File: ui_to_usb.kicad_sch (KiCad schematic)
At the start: 35 parts, among them J1 PM254-2-06-S-8.5, J2 TYPE-C-31-M-12, U1 FT232H, U2 93LCxxB, U3 USBLC6-2SC6, Y2 12M

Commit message: add silkscreen
fix all DRC errors
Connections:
- no-connect marks 2 -> 11
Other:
- moved on the sheet: C1, C5

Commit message: bigger cut-out for LEDs. Add README and renders
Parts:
- D1, D2: footprint LED_SMD:LED_1206_3216Metric_ReverseMount_Hole1.8x2.4mm -> footprints:LED_1206_3216Metric_ReverseMount_Hole2.0x1.6mm

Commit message: check sch and pcb before production, looks ready
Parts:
- R5, R6: value 220R -> 1k5
- R7, R8: value 10k -> 5k1
- U2: value 93LCxxB -> 93LC56B
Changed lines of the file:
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@@
 			)
 		)
-		(property "Value" "93LCxxB"
+		(property "Value" "93LC56B"
 			(at 84.6933 116.84 0)
 			(effects
@@
 			)
 		)
-		(property "Value" "10k"
+		(property "Value" "5k1"
 			(at 62.23 49.53 90)
 			(effects
@@
 			)
 		)
-		(property "Value" "10k"
+		(property "Value" "5k1"
 			(at 62.23 46.99 90)
 			(effects
@@
 			)
 		)
-		(property "Value" "220R"
+		(property "Value" "1k5"
 			(at 198.12 132.08 90)
 			(effects
@@
 			)
 		)
-		(property "Value" "220R"
+		(property "Value" "1k5"
 			(at 198.12 146.05 90)
 			(effects

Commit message: improve BOM, ordered rev -
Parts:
- removed U2: 93LC56B, Package_SO:SOIC-8_3.9x4.9mm_P1.27mm, symbol Memory_EEPROM:93LCxxB
- added U2: 93LC56C, Package_SO:SOIC-8_3.9x4.9mm_P1.27mm, symbol Memory_EEPROM:93LCxxC
- FB1, FB2, FB3, FB4: JLCPCB Part # (none) -> C19330
- U1: footprint Package_QFP:LQFP-48_7x7mm_P0.5mm -> Package_DFN_QFN:QFN-48-1EP_8x8mm_P0.5mm_EP6.2x6.2mm
- Y2: JLCPCB Part # (none) -> C9002
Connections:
- net +3.3V: now also U2.6 (ORG), U2.8 (VCC)
- net EECLK: now also U2.2 (SCLK)
- net EECS: now also U2.1 (CS)
- net GND: now also U2.5 (GND)
- net at R3.2, U1.43 (EEDATA): now also U2.3 (DI)
- net at R3.1, R4.1: now also U2.4 (DO)
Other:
- note added: "16 bit mode"
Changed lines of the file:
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@@
 		(comment 1 "USB adapter for ui_board_1u")
 	)
+	(text "16 bit\nmode"
+		(exclude_from_sim no)
+		(at 73.914 128.27 0)
+		(effects
+			(font
+				(size 1.27 1.27)
+			)
+			(justify right)
+		)
+	)
 	(junction
 		(at 67.31 35.56)
@@
 	)
 	(symbol
-		(lib_id "Memory_EEPROM:93LCxxB")
-		(at 82.55 124.46 0)
-		(unit 1)
-		(exclude_from_sim no)
-		(in_bom yes)
-		(on_board yes)
-		(dnp no)
-		(fields_autoplaced yes)
-		(property "Reference" "U2"
-			(at 84.6933 114.3 0)
-			(effects
-				(font
-					(size 1.27 1.27)
-				)
-				(justify left)
-			)
-		)
-		(property "Value" "93LC56B"
-			(at 84.6933 116.84 0)
-			(effects
-				(font
-					(size 1.27 1.27)
-				)
-				(justify left)
-			)
-		)
-		(property "Footprint" "Package_SO:SOIC-8_3.9x4.9mm_P1.27mm"
-			(at 82.55 124.46 0)
-			(effects
-				(font
-					(size 1.27 1.27)
-				)
-				(hide yes)
-			)
-		)
-		(property "Datasheet" "http://ww1.microchip.com/downloads/en/DeviceDoc/20001749K.pdf"
-			(at 82.55 124.46 0)
-			(effects
-				(font
-					(size 1.27 1.27)
-				)
-				(hide yes)
-			)
-		)
-		(property "Description" "Serial EEPROM, 93 Series, 2.5V, DIP-8/SOIC-8"
-			(at 82.55 124.46 0)
-			(effects
-				(font
-					(size 1.27 1.27)
-				)
-				(hide yes)
-			)
-		)
-		(property "LCSC Part #" ""
-			(at 82.55 124.46 0)
-			(effects
-				(font
-					(size 1.27 1.27)
-				)
-				(hide yes)
-			)
-		)
-		(pin "8"
-		)
-		(pin "7"
-		)
-		(pin "4"
-		)
-		(pin "6"
-		)
-		(pin "5"
-		)
-		(pin "2"
-		)
-		(pin "3"
-		)
-		(pin "1"
-		)
-		(instances
-			(project ""
-				(path "/61164785-2abe-4800-8948-e7ba22968736"
-					(reference "U2")
-					(unit 1)
-				)
-			)
-		)
-	)
-	(symbol
 		(lib_id "power:PWR_FLAG")
 		(at 127 88.9 90)
@@
 			)
 		)
-		(property "Description" "BLM18AG601SN1D"
+		(property "Description" ""
 			(at 154.94 60.96 0)
 			(effects
@@
 			)
 		)
-		(property "LCSC Part #" ""
+		(property "JLCPCB Part #" "C19330"
 			(at 154.94 60.96 0)
 			(effects
@@
 			)
 		)
-		(property "Footprint" "Package_QFP:LQFP-48_7x7mm_P0.5mm"
+		(property "Footprint" "Package_DFN_QFN:QFN-48-1EP_8x8mm_P0.5mm_EP6.2x6.2mm"
 			(at 154.94 116.84 0)
 			(effects
@@
 			)
 		)
-		(property "Description" "BLM18AG601SN1D"
+		(property "Description" ""
 			(at 62.23 41.91 0)
 			(effects
@@
 			)
 		)
-		(property "LCSC Part #" ""
+		(property "JLCPCB Part #" "C19330"
 			(at 62.23 41.91 90)
 			(effects
@@
 			)
 		)
-		(property "LCSC Part #" ""
+		(property "JLCPCB Part #" "C9002"
 			(at 127 134.62 90)
 			(effects
@@
 			)
 		)
-		(property "Description" "BLM18AG601SN1D"
+		(property "Description" ""
 			(at 143.51 60.96 0)
 			(effects
@@
 			)
 		)
-		(property "LCSC Part #" ""
+		(property "JLCPCB Part #" "C19330"
 			(at 143.51 60.96 0)
 			(effects
@@
 	)
 	(symbol
+		(lib_id "Memory_EEPROM:93LCxxC")
+		(at 82.55 124.46 0)
+		(unit 1)
+		(exclude_from_sim no)
+		(in_bom yes)
+		(on_board yes)
+		(dnp no)
+		(property "Reference" "U2"
+			(at 88.138 115.316 0)
+			(effects
+				(font
+					(size 1.27 1.27)
+				)
+				(justify left)
+			)
+		)
+		(property "Value" "93LC56C"
+			(at 88.138 117.856 0)
+			(effects
+				(font
+					(size 1.27 1.27)
+				)
+				(justify left)
+			)
+		)
+		(property "Footprint" "Package_SO:SOIC-8_3.9x4.9mm_P1.27mm"
+			(at 82.55 124.46 0)
+			(effects
+				(font
+					(size 1.27 1.27)
+				)
+				(hide yes)
+			)
+		)
+		(property "Datasheet" "http://ww1.microchip.com/downloads/en/DeviceDoc/20001749K.pdf"
+			(at 82.55 124.46 0)
+			(effects
+				(font
+					(size 1.27 1.27)
+				)
+				(hide yes)
+			)
+		)
+		(property "Description" "Serial EEPROM, 93 Series, with ORG Pin, 2.5V, DIP-8/SOIC-8"
+			(at 82.55 124.46 0)
+			(effects
+				(font
+					(size 1.27 1.27)
+				)
+				(hide yes)
+			)
+		)
+		(pin "1"
+		)
+		(pin "7"
+		)
+		(pin "3"
+		)
+		(pin "5"
+		)
+		(pin "2"
+		)
+		(pin "8"
+		)
+		(pin "6"
+		)
+		(pin "4"
+		)
+		(instances
+			(project ""
+				(path "/61164785-2abe-4800-8948-e7ba22968736"
+					(reference "U2")
+					(unit 1)
+				)
+			)
+		)
+	)
+	(symbol
 		(lib_id "power:GND")
 		(at 114.3 129.54 270)
@@
 	(symbol
 		(lib_id "power:+3.3V")
+		(at 72.39 124.46 90)
+		(unit 1)
+		(exclude_from_sim no)
+		(in_bom yes)
+		(on_board yes)
+		(dnp no)
+		(property "Reference" "#PWR051"
+			(at 76.2 124.46 0)
+			(effects
+				(font
+					(size 1.27 1.27)
+				)
+				(hide yes)
+			)
+		)
+		(property "Value" "+3.3V"
+			(at 66.548 124.206 90)
+			(effects
+				(font
+					(size 1.27 1.27)
+				)
+			)
+		)
+		(property "Footprint" ""
+			(at 72.39 124.46 0)
+			(effects
+				(font
+					(size 1.27 1.27)
+				)
+				(hide yes)
+			)
+		)
+		(property "Datasheet" ""
+			(at 72.39 124.46 0)
+			(effects
+				(font
+					(size 1.27 1.27)
+				)
+				(hide yes)
+			)
+		)
+		(property "Description" "Power symbol creates a global label with name \"+3.3V\""
+			(at 72.39 124.46 0)
+			(effects
+				(font
+					(size 1.27 1.27)
+				)
+				(hide yes)
+			)
+		)
+		(pin "1"
+		)
+		(instances
+			(project "ui_to_usb"
+				(path "/61164785-2abe-4800-8948-e7ba22968736"
+					(reference "#PWR051")
+					(unit 1)
+				)
+			)
+		)
+	)
+	(symbol
+		(lib_id "power:+3.3V")
 		(at 160.02 78.74 0)
 		(unit 1)
@@
 			)
 		)
-		(property "Description" "BLM18AG601SN1D"
+		(property "Description" ""
 			(at 62.23 35.56 0)
 			(effects
@@
 			)
 		)
-		(property "LCSC Part #" ""
+		(property "JLCPCB Part #" "C19330"
 			(at 62.23 35.56 90)
 			(effects

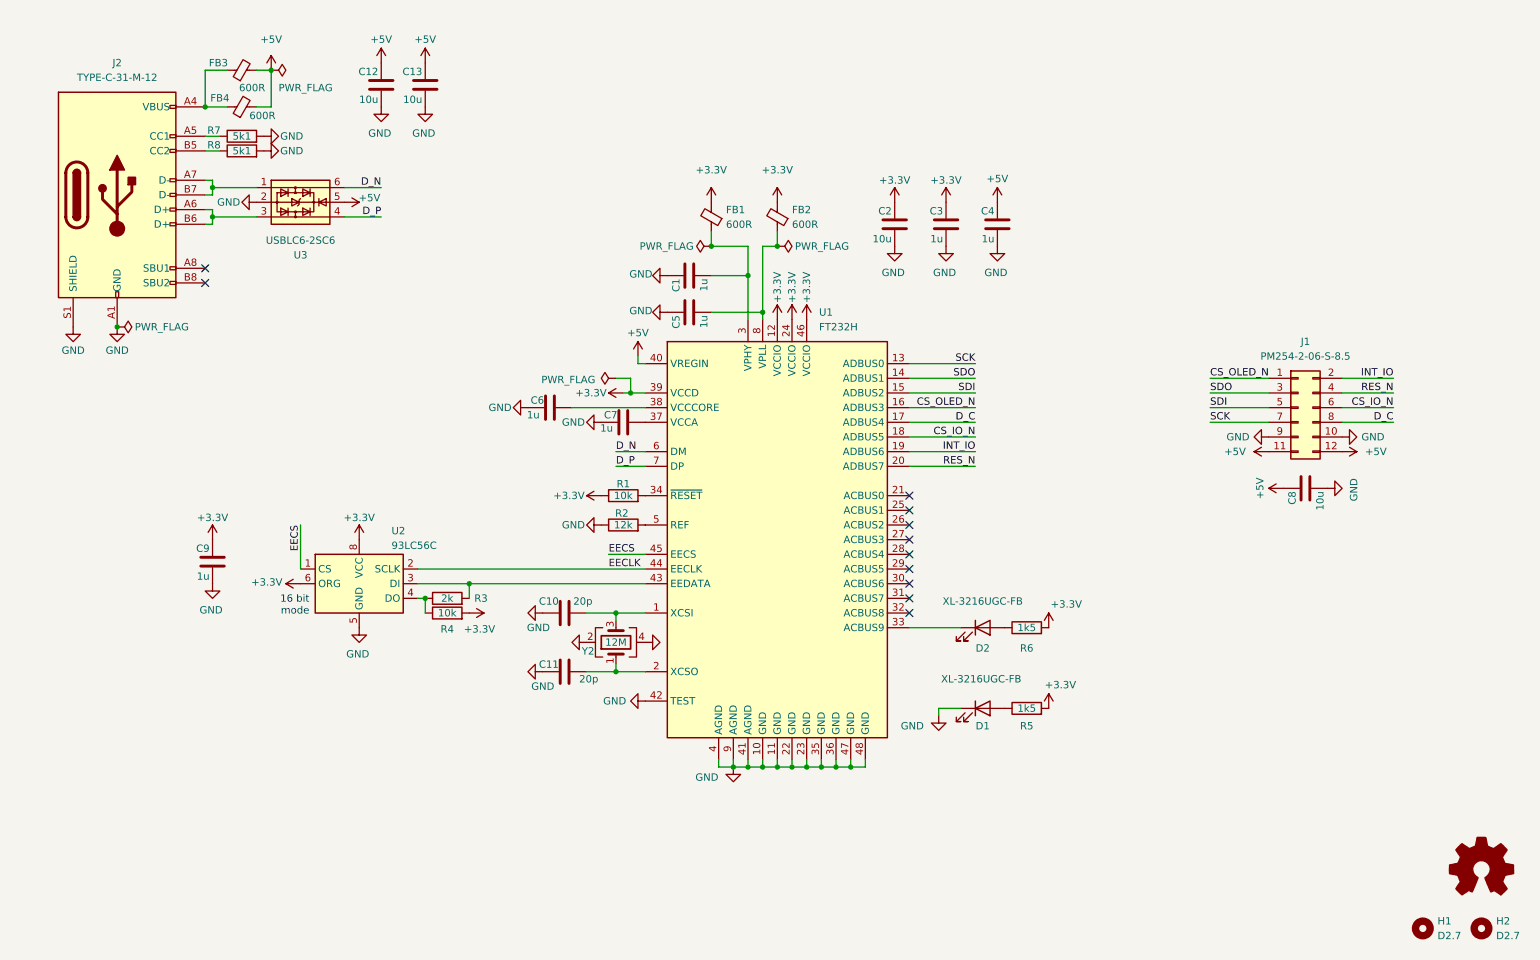
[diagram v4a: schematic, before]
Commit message: add CH32V305G (QFN28) symbol
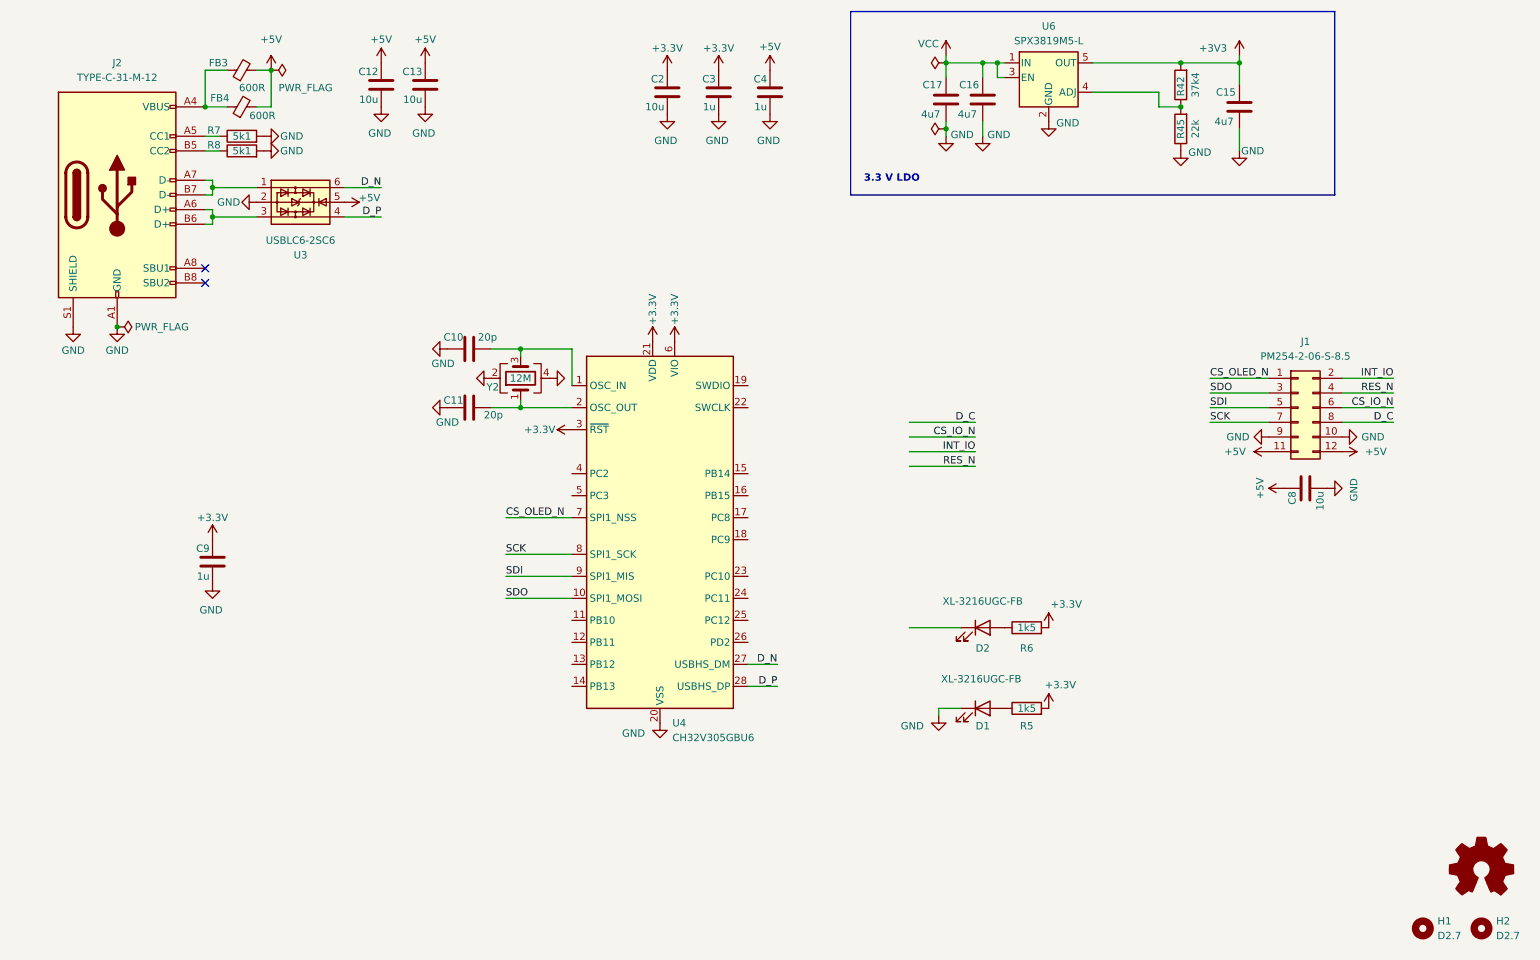
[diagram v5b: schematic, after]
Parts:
- removed C1, C5, C6, C7: 1u, Capacitor_SMD:C_0603_1608Metric, symbol Device:C
- removed FB1, FB2: 600R, Inductor_SMD:L_0603_1608Metric, symbol Device:FerriteBead_Small
- removed R1, R4: 10k, Resistor_SMD:R_0603_1608Metric, symbol Device:R
- removed R2: 12k, Resistor_SMD:R_0603_1608Metric, symbol Device:R
- removed R3: 2k, Resistor_SMD:R_0603_1608Metric, symbol Device:R
- removed U1: FT232H, Package_DFN_QFN:QFN-48-1EP_8x8mm_P0.5mm_EP6.2x6.2mm, symbol Interface_USB:FT232H
- removed U2: 93LC56C, Package_SO:SOIC-8_3.9x4.9mm_P1.27mm, symbol Memory_EEPROM:93LCxxC
- added C15, C16, C17: 4u7, Capacitor_SMD:C_1206_3216Metric, symbol Device:C
- added R42: 37k4, Resistor_SMD:R_0603_1608Metric, symbol Device:R
- added R45: 22k, Resistor_SMD:R_0603_1608Metric, symbol Device:R
- added U4: CH32V305GBU6, Package_DFN_QFN:QFN-28-1EP_4x4mm_P0.4mm_EP2.3x2.3mm, symbol lib:CH32V305GBU6
- added U6: SPX3819M5-L, Package_TO_SOT_SMD:SOT-23-5, symbol Regulator_Linear:SPX3819M5-L
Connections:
- net +3.3V: now also U4.21 (VDD), U4.3 (~{RST}), U4.6 (VIO)
- net CS_OLED_N: now also U4.7 (PA4)
- net D_N: now also U4.27 (PB6)
- net D_P: now also U4.28 (PB7)
- net GND: now also C15.2, C16.2, C17.2, R45.1, U4.0 (VSS), U4.20 (VSS), U6.2 (GND)
- net SCK: now also U4.8 (PA5)
- net SDI: now also U4.9 (PA6)
- net SDO: now also U4.10 (PA7)
- net at C10.2, Y2.3: now also U4.1 (OSC_IN)
- net at C11.2, Y2.1: now also U4.2 (OSC_OUT)
- new net: R42.1, R45.2, U6.4 (ADJ)
- new net +3V3: C15.1, R42.2, U6.5 (OUT)
- new net VCC: C16.1, C17.1, U6.1 (IN), U6.3 (EN)
- no-connect marks 11 -> 2
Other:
- note added: "3.3 V LDO"
- note removed: "16 bit mode"
- moved on the sheet: C10, C11, C2, C3, C4, Y2

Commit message: schematic progress
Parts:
- Y2: value 12M -> 8M; JLCPCB Part # C9002 -> C2682774
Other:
- note added: "ADD Buttons * RESET * BOOTLOAD"
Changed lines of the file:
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@@
 		)
 	)
+	(text "ADD Buttons\n  * RESET\n  * BOOTLOAD"
+		(exclude_from_sim no)
+		(at 134.874 164.846 0)
+		(effects
+			(font
+				(size 1.27 1.27)
+			)
+			(justify left)
+		)
+	)
 	(text "3.3 V LDO"
 		(exclude_from_sim no)
@@
 			)
 		)
-		(property "Value" "12M"
+		(property "Value" "8M"
 			(at 110.49 88.9 90)
 			(effects
@@
 			)
 		)
-		(property "Datasheet" "https://jlcpcb.com/partdetail/YXC_CrystalOscillators-X322512MSB4SI/C9002"
+		(property "Datasheet" "https://jlcpcb.com/partdetail/2777871-X32258MSB4SI/C2682774"
 			(at 110.49 88.9 0)
 			(effects
@@
 			)
 		)
-		(property "JLCPCB Part #" "C9002"
+		(property "JLCPCB Part #" "C2682774"
 			(at 110.49 88.9 90)
 			(effects
